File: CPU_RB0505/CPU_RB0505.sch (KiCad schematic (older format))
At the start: 0 parts

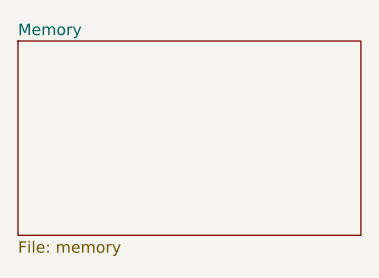
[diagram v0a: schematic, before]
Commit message: Update Memory page of CPU
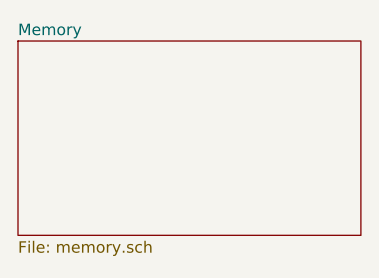
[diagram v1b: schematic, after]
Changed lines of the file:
@@
 U 5E8CCFC8
 F0 "Memory" 50
-F1 "memory" 50
+F1 "memory.sch" 50
 $EndSheet
 $EndSCHEMATC
